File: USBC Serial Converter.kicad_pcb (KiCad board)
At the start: 2 copper layers, 39.5 x 19.5 mm, 18 parts, among them IC1 AP2112M-3.3TRG1, J1 Conn_01x04_Pin, J2 Conn_01x03_Pin, J3 USB_C_Receptacle_USB2.0_16P, U1 CH340C

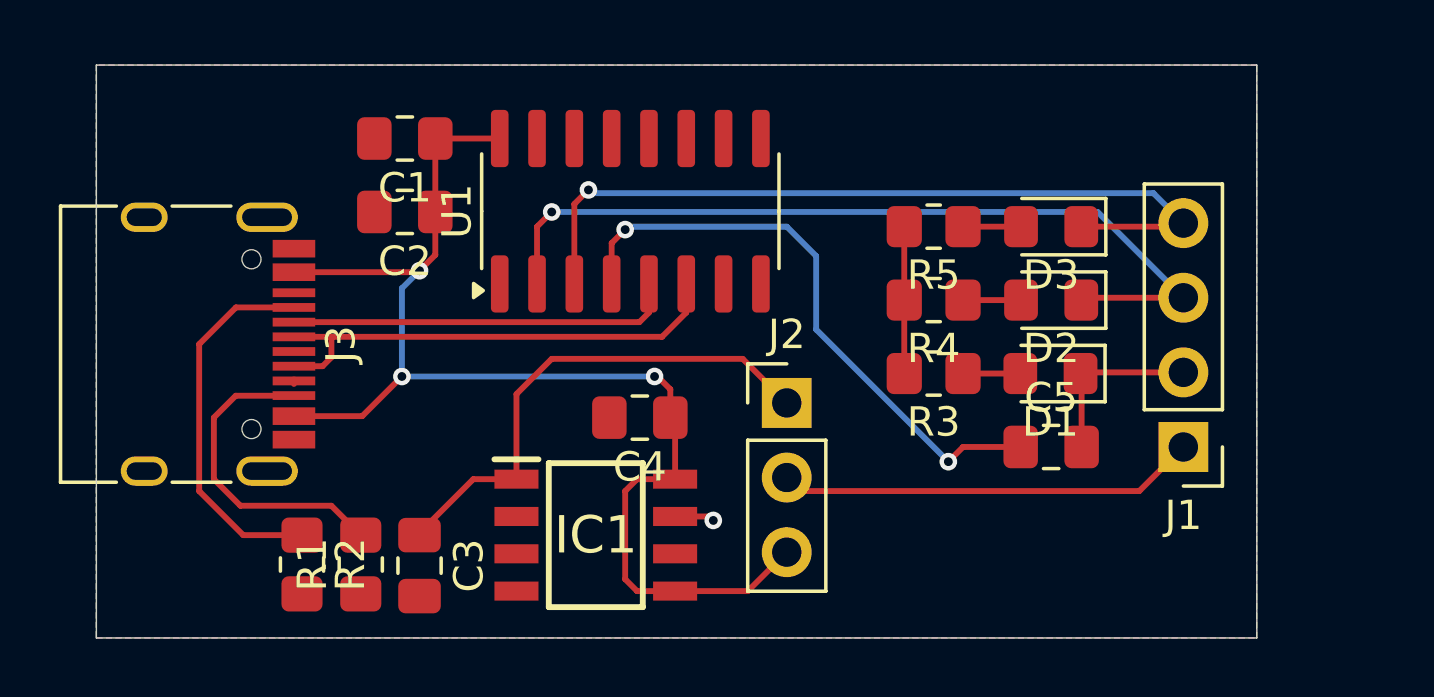
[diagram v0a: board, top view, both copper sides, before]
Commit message: added isolater for future
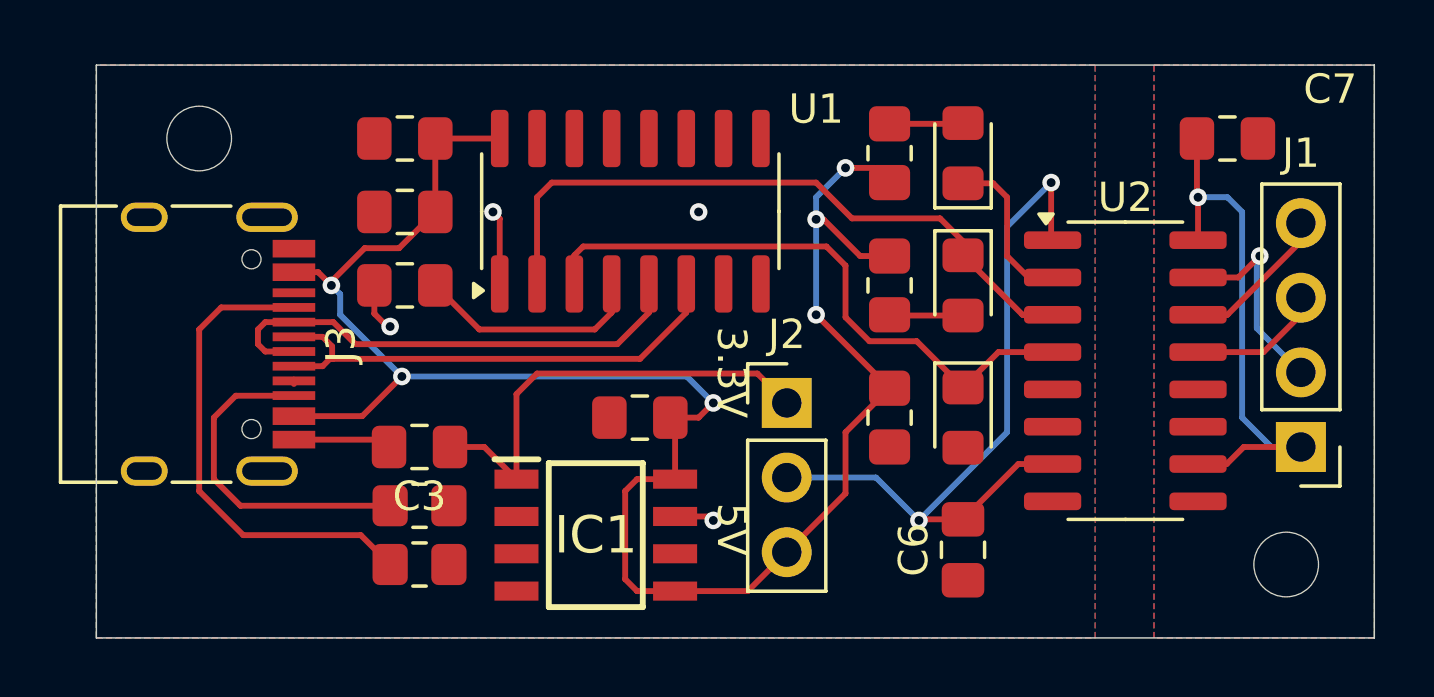
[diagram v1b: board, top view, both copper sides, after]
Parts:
- added C6: 0.1u, Capacitor_SMD:C_0805_2012Metric_Pad1.18x1.45mm_HandSolder, F.Cu at (76.0, 95.5)
- added C7: 0.1u, Capacitor_SMD:C_0805_2012Metric_Pad1.18x1.45mm_HandSolder, F.Cu at (85.0, 81.5)
- added H1: MountingHole, MountingHole:MountingHole_2.2mm_M2_ISO7380, F.Cu at (87.0, 96.0)
- added H1: MountingHole, MountingHole:MountingHole_2.2mm_M2_ISO7380, F.Cu at (50.0, 81.5)
- added U2: Si8642BC-B-IS1, Package_SO:SOIC-16_3.9x9.9mm_P1.27mm, F.Cu at (81.5, 89.4)
- moved C5 22.7 mm to (57.0, 86.5), turned to 180 degrees
- moved D1 8.07 mm to (76.0, 82.0), turned to 90 degrees
- moved R3 7.65 mm to (73.5, 82.0), turned to -90 degrees
- moved D3 7.16 mm to (76.0, 91.0), turned to -90 degrees
- moved R5 6.67 mm to (73.5, 91.0), turned to 90 degrees
- moved C3 4.04 mm to (57.5, 92.0), turned to 180 degrees
- moved J1 4.00 mm to (87.5, 92.0)
- moved R2 4.00 mm to (57.5, 96.0), turned to 0 degrees
- moved D2 3.04 mm to (76.0, 86.5), turned to -90 degrees
- moved R1 2.83 mm to (57.5, 94.0), turned to 180 degrees
- moved R4 1.58 mm to (73.5, 86.5), turned to 90 degrees
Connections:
- J1 pad 1: VCOM -> VCOM_B
- J1 pad 2: GND -> GND_B
- J1 pad 3: /TXD -> /RXD_B
- J1 pad 4: /RXD -> /TXD_B
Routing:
- net VCOM_B: track 0.00 -> 18.3 mm, vias 0 -> 1
- net +5V: track 48.4 -> 66.2 mm, vias 3 -> 6
- net Net-(U1-V3): track 20.6 -> 7.84 mm, vias 2 -> 0
- net VCOM: track 14.3 -> 26.4 mm, vias 0 -> 2
- net GND: track 7.39 -> 14.6 mm, vias 1 -> 4
- net GND_B: track 0.00 -> 7.08 mm, vias 0 -> 1
- net /RXD: track 27.6 -> 20.9 mm, vias 1 -> 0
- net /TXD: track 28.9 -> 22.8 mm, vias 1 -> 0
- net /TXD_B: track 0.00 -> 5.16 mm
- net /RXD_B: track 0.00 -> 4.61 mm
- net /USBD-: track 13.2 -> 17.0 mm
- net Net-(J3-CC1): track 12.9 -> 16.6 mm
- net Net-(D3-A): track 1.97 -> 0.00 mm
- net +3.3V: track 17.5 -> 15.5 mm
- net Net-(J3-CC2): track 10.9 -> 11.5 mm
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- added copper zone on B.Cu, net GND_B
- added copper zone on F.Cu, net GND_B
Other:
- board size 39.5 x 19.5 mm -> 43.5 x 19.5 mm
- board text added: "3.3V"
- board text added: "5V"
